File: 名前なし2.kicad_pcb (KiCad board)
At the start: 2 copper layers, 85 x 50 mm, 69 parts, among them IC1 SI8650AB-B-IS1, IC2 A3921KLPTR-T, IC3 SI8650AB-B-IS1, IC4 A3921KLPTR-T, J1 Conn_01x02, J2 Conn_01x03, J3 Conn_01x05, J4 Conn_01x02, J5 Bus_mechaken_PCIexpress_x16_1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, Q1 NVMFD5C446NT1G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

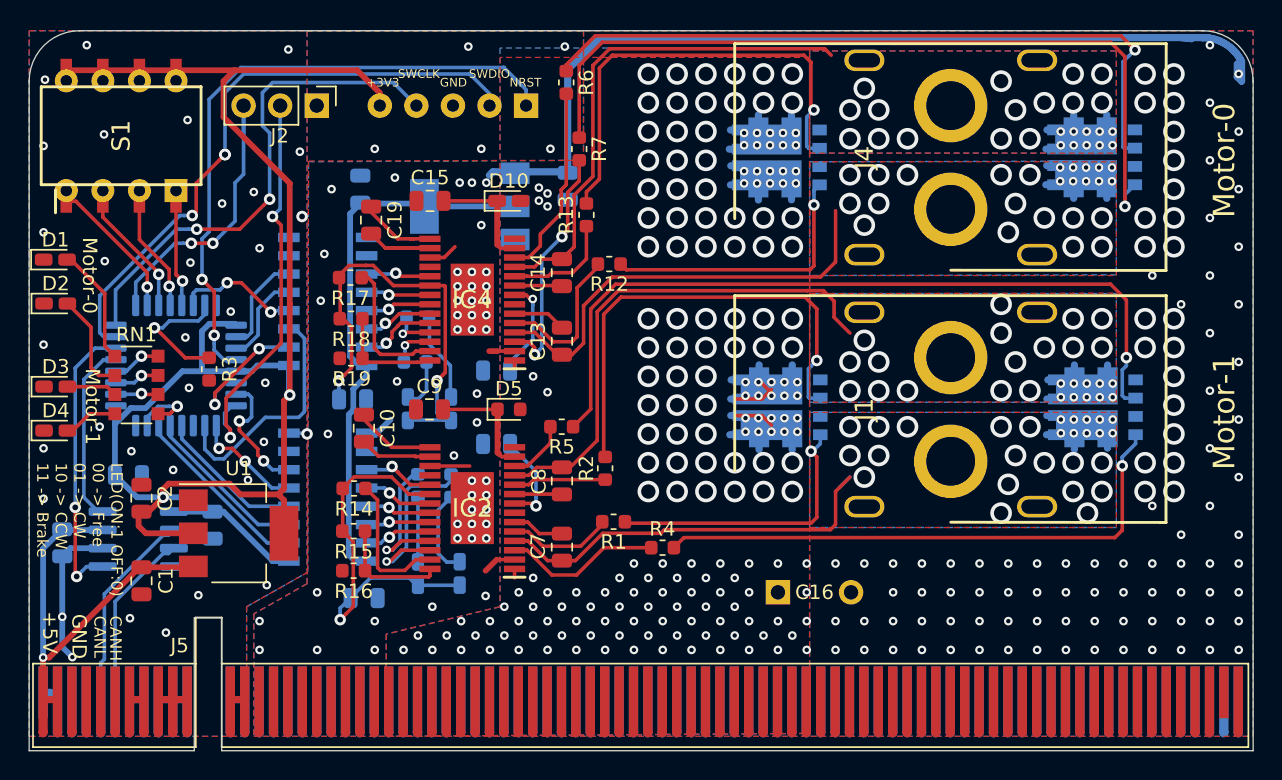
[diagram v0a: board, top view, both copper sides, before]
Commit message: change
FET等の裏表反転
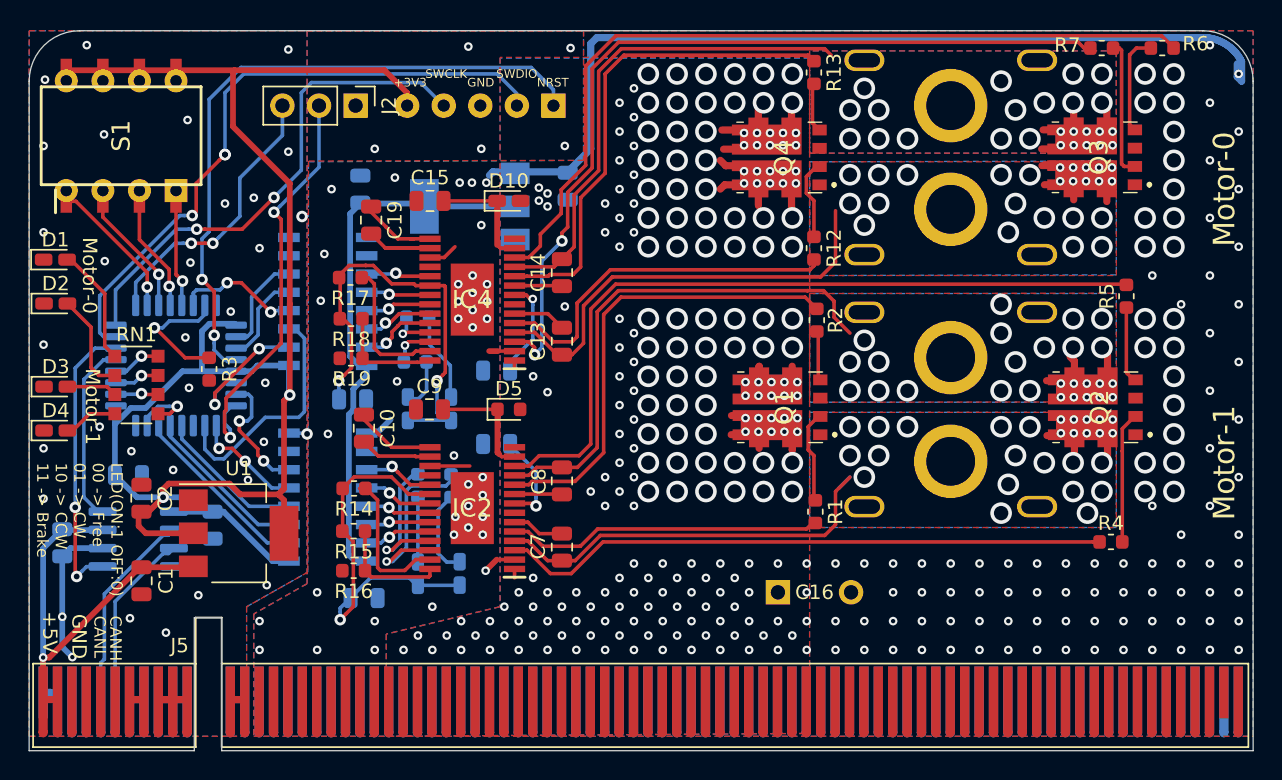
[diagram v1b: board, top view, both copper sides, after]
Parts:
- C16, Q1, Q2, Q3, Q4: moved to F.Cu
- J1, J4: moved to B.Cu
- moved R6 41.5 mm to (128.7, 41.2), turned to 180 degrees
- moved R5 40.2 mm to (126.2, 58.4), turned to 90 degrees
- moved R7 37.0 mm to (124.5, 41.2), turned to 180 degrees
- moved R4 31.1 mm to (125.1, 75.5)
- moved R13 18.6 mm to (104.5, 42.9), turned to 90 degrees
- moved R2 17.9 mm to (104.7, 60.1), turned to 90 degrees
- moved R12 14.3 mm to (104.5, 55.1), turned to 90 degrees
- moved R1 14.0 mm to (104.6, 73.4), turned to 90 degrees
- moved J2 2.70 mm to (72.7, 45.2)
- moved J3 1.90 mm to (86.4, 45.2)
- turned C16 to 90 degrees
- turned J1 to 270 degrees
- turned J4 to 270 degrees
- turned Q1 to 90 degrees
- turned Q2 to 90 degrees
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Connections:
- J1 pad 1: SB_1 -> SA_1
- J1 pad 2: SA_1 -> SB_1
- J4 pad 1: SB_0 -> SA_0
- J4 pad 2: SA_0 -> SB_0
- Q1 pad 1: SA_1 -> SB_1
- Q1 pad 3: SB_1 -> SA_1
- Q2 pad 5: SB_1 -> SA_1
- Q2 pad 6: SA_1 -> SB_1
- Q3 pad 5: SB_0 -> SA_0
- Q3 pad 6: SA_0 -> SB_0
- Q4 pad 1: SA_0 -> SB_0
- Q4 pad 3: SB_0 -> SA_0
- R1 pad 2: Net-(Q1-Pad4) -> Net-(Q1-Pad2)
- R12 pad 2: Net-(Q4-Pad4) -> Net-(Q4-Pad2)
- R13 pad 1: Net-(Q4-Pad2) -> Net-(Q4-Pad4)
- R2 pad 1: Net-(Q1-Pad2) -> Net-(Q1-Pad4)
- R4 pad 2: Net-(Q2-Pad4) -> Net-(Q2-Pad2)
- R5 pad 1: Net-(Q2-Pad2) -> Net-(Q2-Pad4)
- R6 pad 2: Net-(Q3-Pad2) -> Net-(Q3-Pad4)
- R7 pad 1: Net-(Q3-Pad4) -> Net-(Q3-Pad2)
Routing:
- net Net-(Q3-Pad4): track 56.2 -> 7.03 mm, vias 1 -> 0
- net GLA_1: track 4.28 -> 53.2 mm
- net Net-(Q2-Pad2): track 54.8 -> 9.00 mm, vias 1 -> 0
- net GLA_0: track 13.4 -> 58.0 mm
- net GLB_0: track 16.8 -> 59.1 mm
- net Net-(Q3-Pad2): track 49.1 -> 9.55 mm, vias 1 -> 0
- net Net-(Q2-Pad4): track 38.7 -> 5.25 mm, vias 1 -> 0
- net GLB_1: track 11.0 -> 42.6 mm
- net Net-(Q4-Pad2): track 32.1 -> 5.61 mm, vias 1 -> 0
- net GHA_0: track 7.76 -> 34.2 mm
- net Net-(Q1-Pad2): track 32.5 -> 6.44 mm, vias 1 -> 0
- net GHA_1: track 6.44 -> 32.3 mm
- net Net-(Q1-Pad4): track 19.7 -> 3.46 mm, vias 1 -> 0
- net Net-(Q4-Pad4): track 19.5 -> 3.68 mm, vias 1 -> 0
- net GHB_0: track 10.7 -> 25.3 mm
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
